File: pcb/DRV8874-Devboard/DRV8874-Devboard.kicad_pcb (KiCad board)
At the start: 4 copper layers, 65 x 67 mm, 55 parts, among them J1 Conn_01x04_Pin, J10 Conn_01x06_Pin, J12 Conn_01x03_Pin, J2 Screw_Terminal_01x02, J3 Conn_01x03_Pin, J4 Conn_01x03_Pin, J5 Conn_01x04_Pin, J6 Conn_01x03_Pin, J7 Conn_01x03_Pin, J9 Conn_01x03_Pin, U1 DRV8874, U2 BL9342, U3 DRV8874, U4 SN65HVD230, U5 TPS16630PWPR, U6 M95320-WMN6TP, U7 TinyThinker_J1

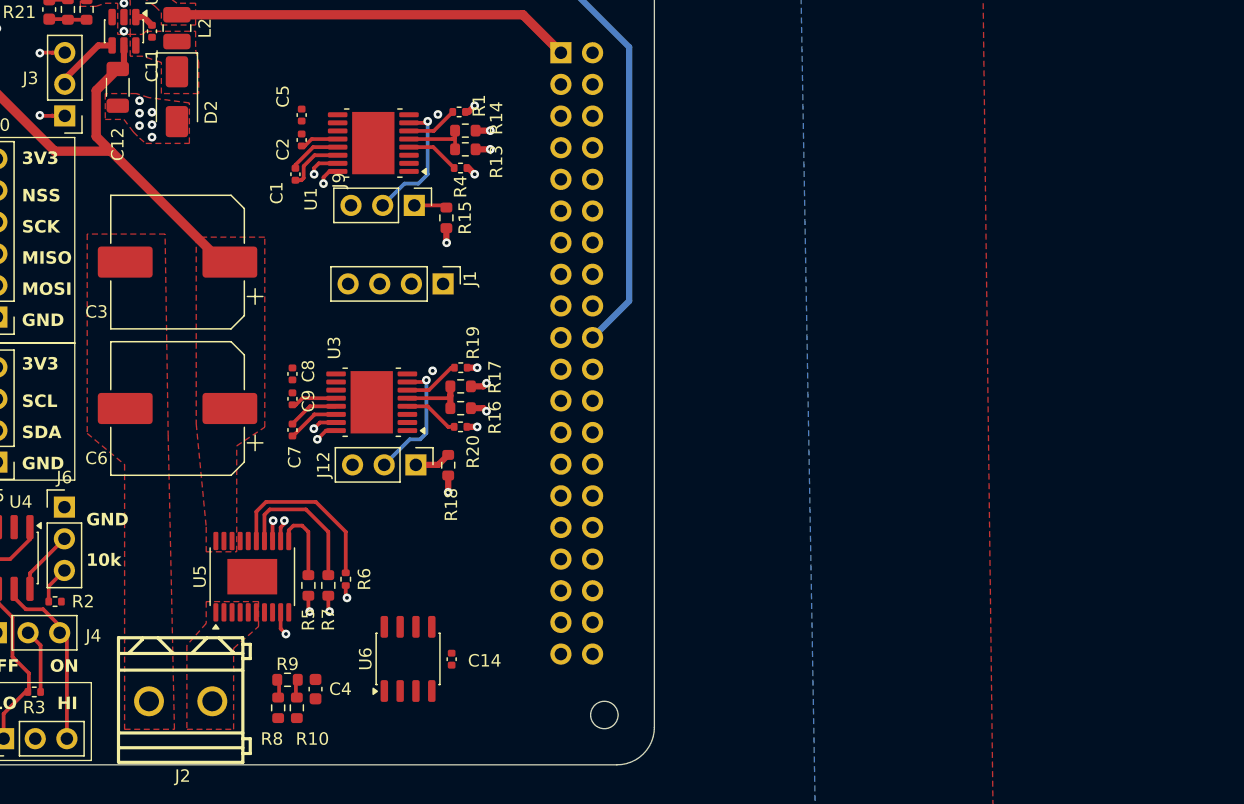
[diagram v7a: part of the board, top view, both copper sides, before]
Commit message: updated EEPROM in schematic
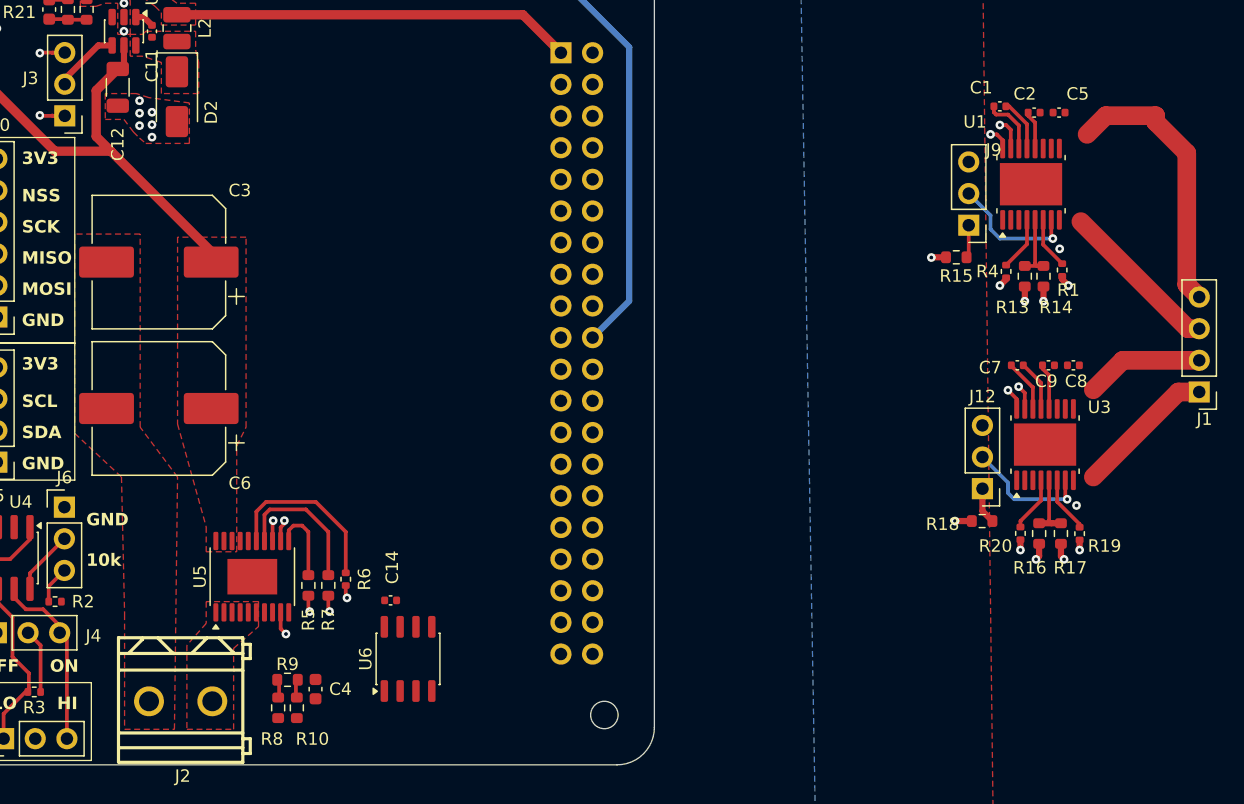
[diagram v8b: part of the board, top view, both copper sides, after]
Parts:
- R7: value 20k -> 18k
- moved C8 62.7 mm to (195.4, 74.5), turned to 0 degrees
- moved J1 61.3 mm to (205.5, 76.7), turned to 180 degrees
- moved C5 60.8 mm to (194.2, 54.2), turned to 0 degrees
- moved C9 60.7 mm to (193.4, 74.5), turned to 180 degrees
- moved C2 58.8 mm to (192.2, 54.2), turned to 180 degrees
- moved C7 58.4 mm to (190.9, 74.5), turned to 180 degrees
- moved C1 56.8 mm to (189.5, 53.8), turned to 180 degrees
- moved U3 54.1 mm to (193.1, 80.9), turned to 90 degrees
- moved U1 52.9 mm to (192.0, 60.0), turned to 90 degrees
- moved R19 51.4 mm to (195.9, 88.0), turned to -90 degrees
- moved R1 50.0 mm to (194.5, 66.9), turned to -90 degrees
- moved R17 49.6 mm to (194.4, 88.0), turned to -90 degrees
- moved R14 47.9 mm to (193.0, 67.4), turned to -90 degrees
- moved R16 47.5 mm to (192.7, 88.0), turned to 90 degrees
- moved R13 46.0 mm to (191.5, 67.4), turned to 90 degrees
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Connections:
- U6 pad 3: unconnected-(U6-W-Pad3) -> +3.3V
- U6 pad 7: unconnected-(U6-HOLD-Pad7) -> +3.3V
- U7 pad 24: unconnected-(U7A-ADC1_IN14-Pad24) -> /TPS_MON
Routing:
- net /A_OUT-: track 0.00 -> 22.1 mm
- net /A_OUT+: track 0.00 -> 13.1 mm
- net /B_OUT+: track 0.00 -> 11.3 mm
- net /B_OUT-: track 0.00 -> 9.48 mm
